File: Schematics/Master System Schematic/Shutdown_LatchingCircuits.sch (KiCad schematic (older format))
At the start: 6 parts, among them K10 Omron DPDT Relay, K7 Omron DPDT Relay, K8 Omron DPDT Relay, K9 Omron DPDT Relay

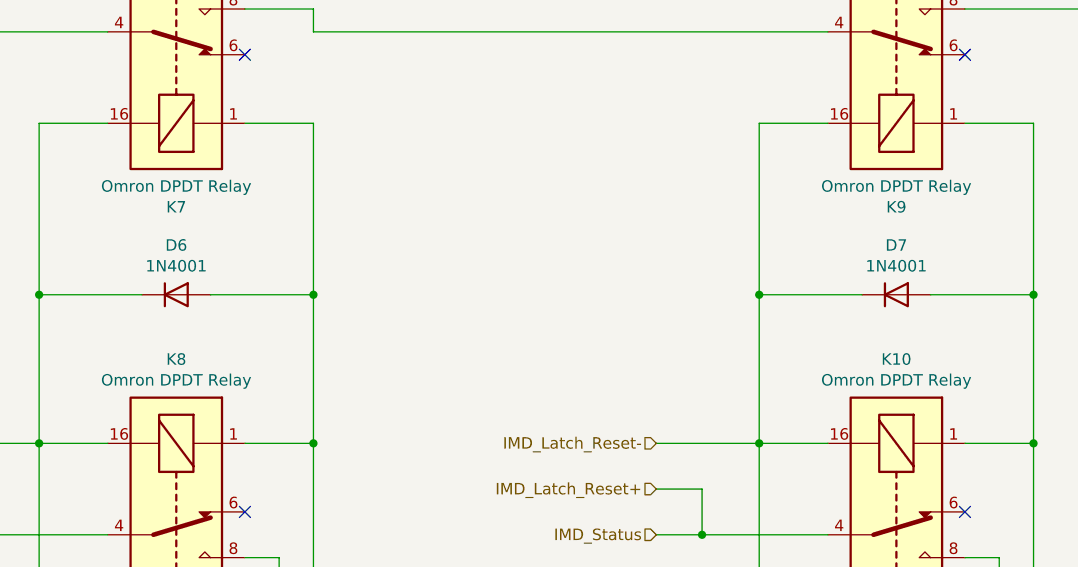
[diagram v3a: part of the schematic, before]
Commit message: Had to refactor all IDs
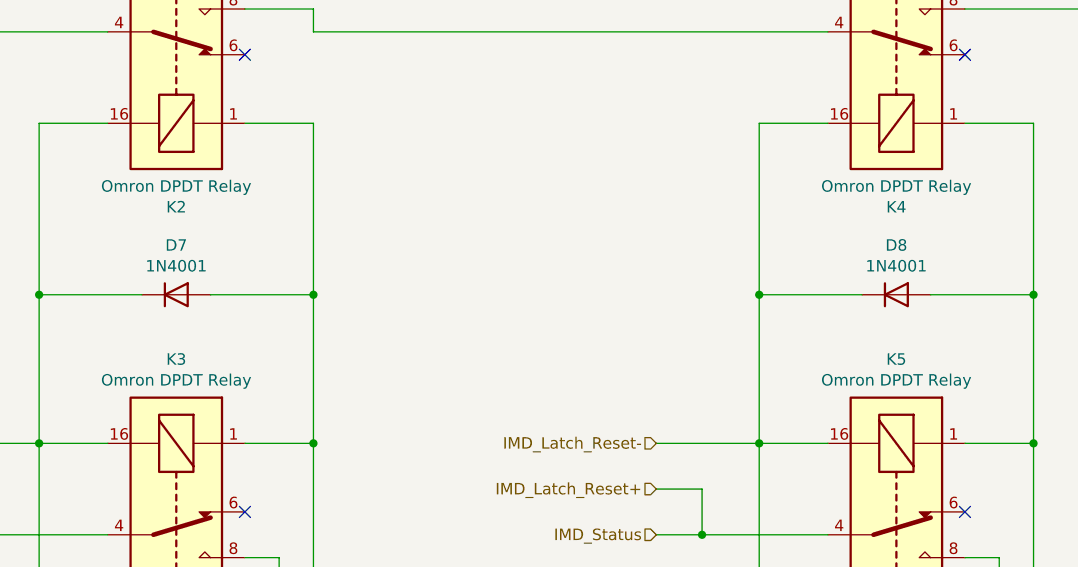
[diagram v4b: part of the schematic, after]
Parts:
- renumbered D6 to D7, D7 to D8, K7 to K2, K8 to K3, K9 to K4, K10 to K5
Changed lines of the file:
@@
 $Descr A 11000 8500
 encoding utf-8
-Sheet 2 17
+Sheet 2 21
 Title "Shutdown Latching Circuits"
 Date "2020-10-12"
@@
 Ground
 $Comp
-L Relay:G5V-2 K10
+L Relay:G5V-2 K5
 U 1 1 5F6E0AD1
 P 7350 4850
-F 0 "K10" V 6583 4850 50  0000 C CNN
+F 0 "K5" V 6583 4850 50  0000 C CNN
 F 1 "Omron DPDT Relay" V 6674 4850 50  0000 C CNN
 F 2 "Relay_THT:Relay_DPDT_Omron_G5V-2" H 8000 4800 50  0001 L CNN
@@
 $EndComp
 $Comp
-L Relay:G5V-2 K9
+L Relay:G5V-2 K4
 U 1 1 5F6E0AD7
 P 7350 2650
-F 0 "K9" V 6583 2650 50  0000 C CNN
+F 0 "K4" V 6583 2650 50  0000 C CNN
 F 1 "Omron DPDT Relay" V 6674 2650 50  0000 C CNN
 F 2 "Relay_THT:Relay_DPDT_Omron_G5V-2" H 8000 2600 50  0001 L CNN
@@
 $EndComp
 $Comp
-L Diode:1N4001 D7
+L Diode:1N4001 D8
 U 1 1 5F6E5F37
 P 7350 3800
-F 0 "D7" H 7350 4016 50  0000 C CNN
+F 0 "D8" H 7350 4016 50  0000 C CNN
 F 1 "1N4001" H 7350 3925 50  0000 C CNN
 F 2 "Diode_THT:D_DO-41_SOD81_P10.16mm_Horizontal" H 7350 3625 50  0001 C CNN
@@
 	3150 4650 3350 4650
 $Comp
-L Relay:G5V-2 K8
+L Relay:G5V-2 K3
 U 1 1 5F7C981B
 P 4200 4850
-F 0 "K8" V 3433 4850 50  0000 C CNN
+F 0 "K3" V 3433 4850 50  0000 C CNN
 F 1 "Omron DPDT Relay" V 3524 4850 50  0000 C CNN
 F 2 "Relay_THT:Relay_DPDT_Omron_G5V-2" H 4850 4800 50  0001 L CNN
@@
 $EndComp
 $Comp
-L Relay:G5V-2 K7
+L Relay:G5V-2 K2
 U 1 1 5F7C9821
 P 4200 2650
-F 0 "K7" V 3433 2650 50  0000 C CNN
+F 0 "K2" V 3433 2650 50  0000 C CNN
 F 1 "Omron DPDT Relay" V 3524 2650 50  0000 C CNN
 F 2 "Relay_THT:Relay_DPDT_Omron_G5V-2" H 4850 2600 50  0001 L CNN
@@
 $EndComp
 $Comp
-L Diode:1N4001 D6
+L Diode:1N4001 D7
 U 1 1 5F7C9827
 P 4200 3800
-F 0 "D6" H 4200 4016 50  0000 C CNN
+F 0 "D7" H 4200 4016 50  0000 C CNN
 F 1 "1N4001" H 4200 3925 50  0000 C CNN
 F 2 "Diode_THT:D_DO-41_SOD81_P10.16mm_Horizontal" H 4200 3625 50  0001 C CNN
